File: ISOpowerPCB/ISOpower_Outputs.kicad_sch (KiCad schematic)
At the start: 53 parts

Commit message: deleted old backups & added documentation
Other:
- note added: "THis is all wrong, needs 12v drivers]"
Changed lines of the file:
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@@
     (effects (font (size 0.8 0.8)) (justify left bottom))
+  )
+  (text "THis is all wrong, needs 12v drivers]\n" (at 201.93 154.94 0)
+    (effects (font (size 2.5 2.5)) (justify left bottom))
   )
   (text "USB Control Logic" (at 40.64 71.12 0)

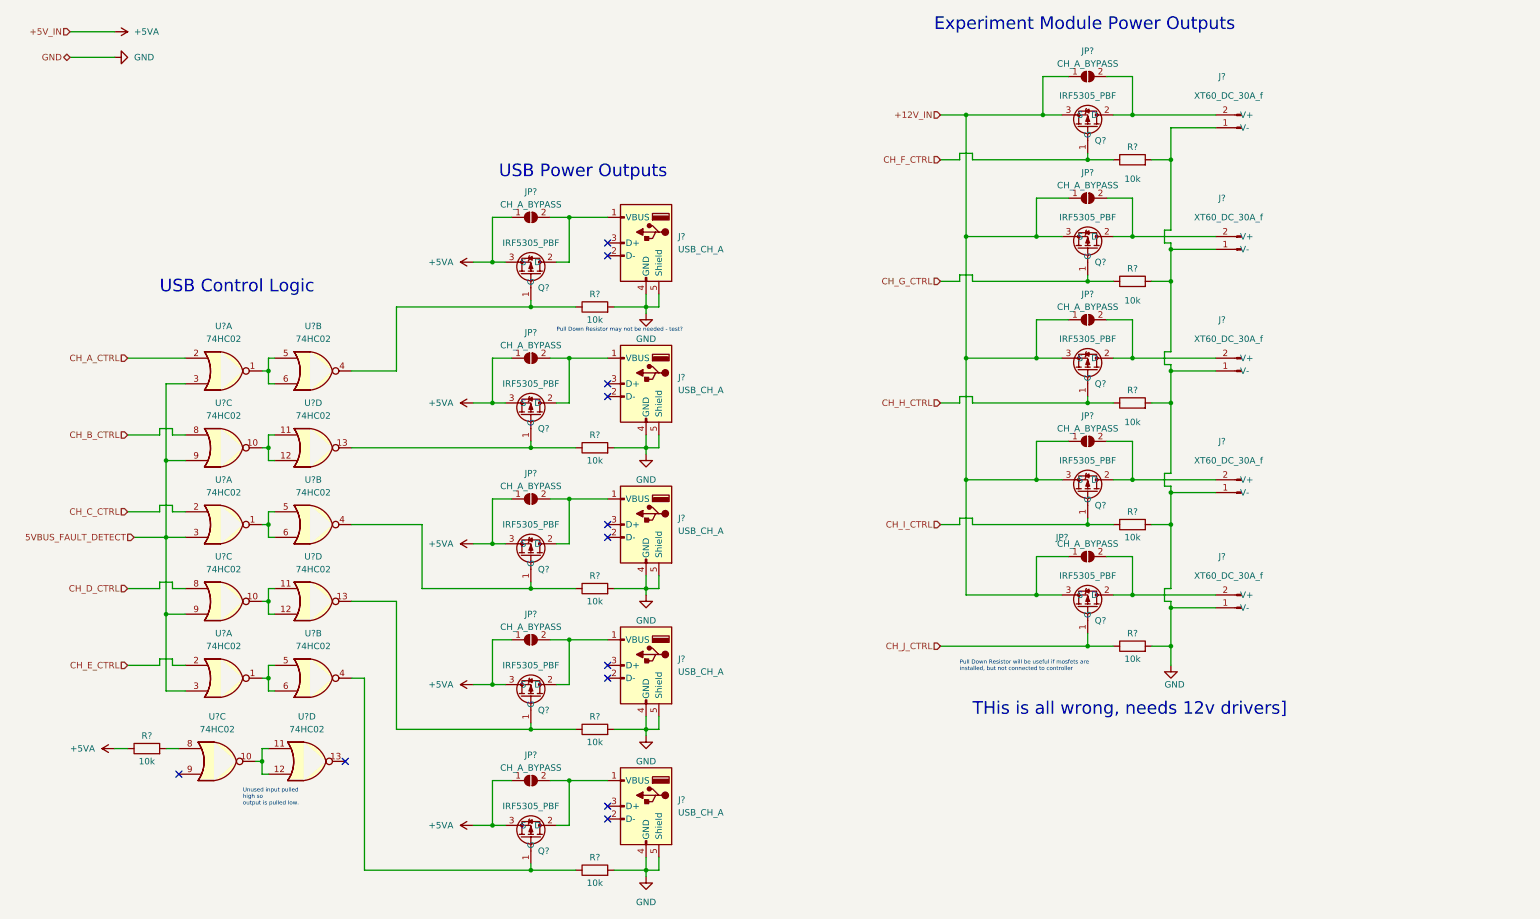
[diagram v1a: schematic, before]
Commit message: Finished initial circuit design
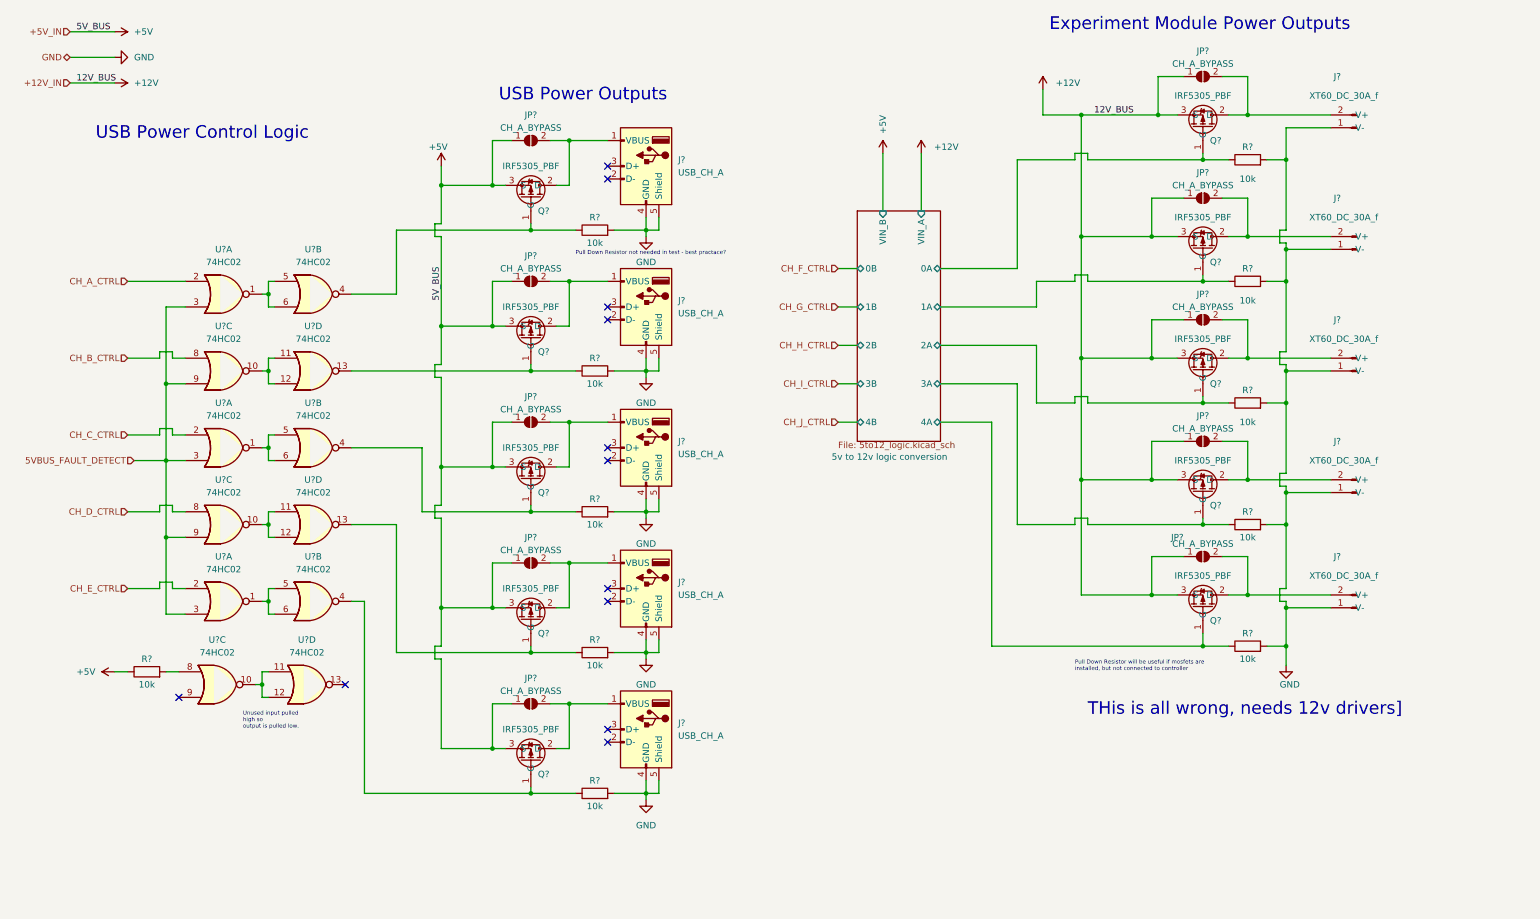
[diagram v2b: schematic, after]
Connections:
- net CH_F_CTRL: no longer Q?.1 (G), R?.1
- net CH_G_CTRL: no longer Q?.1 (G), R?.1
- net CH_H_CTRL: no longer Q?.1 (G), R?.1
- net CH_I_CTRL: no longer Q?.1 (G), R?.1
- net CH_J_CTRL: no longer Q?.1 (G), R?.1
- net +12V_IN renamed +12V
- net +5VA renamed +5V
- new net 5v to 12v logic conversion/0A: Q?.1 (G), R?.1
- new net 5v to 12v logic conversion/1A: Q?.1 (G), R?.1
- new net 5v to 12v logic conversion/2A: Q?.1 (G), R?.1
- new net 5v to 12v logic conversion/3A: Q?.1 (G), R?.1
- new net 5v to 12v logic conversion/4A: Q?.1 (G), R?.1
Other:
- added sheet 5v to 12v logic conversion (5to12_logic.kicad_sch)
- note added: "Pull Down Resistor not needed in test - best practace?"
- note added: "USB Power Control Logic"
- note removed: "Pull Down Resistor may not be needed - test?"
- note removed: "USB Control Logic"
- moved on the sheet: J?, JP?, Q?, R?, U?A, U?B, U?C, U?D

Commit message: Major schematic revisions
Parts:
- removed JP? (x5): CH_A_BYPASS, symbol Jumper:SolderJumper_2_Open
- removed Q? (x5): IRF5305_PBF, Package_TO_SOT_THT:TO-220-3_Vertical, symbol 000_MOSFET_Immo:IRF5305_PBF
- removed R? (x6): 10k, Resistor_SMD:R_0805_2012Metric_Pad1.20x1.40mm_HandSolder, symbol 000_Resistors_Immo:Resistor_0805
- removed U? (x12): 74HC02, symbol 74xx:74HC02
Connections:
- net +5V: now also J?.1 (VBUS), J?.1 (VBUS), J?.1 (VBUS), J?.1 (VBUS), J?.1 (VBUS)
- no-connect marks 12 -> 10
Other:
- note removed: "Pull Down Resistor not needed in test - best practace?"
- note removed: "USB Power Control Logic"
- note removed: "Unused input pulled high so output is pulled low."
- moved on the sheet: J?

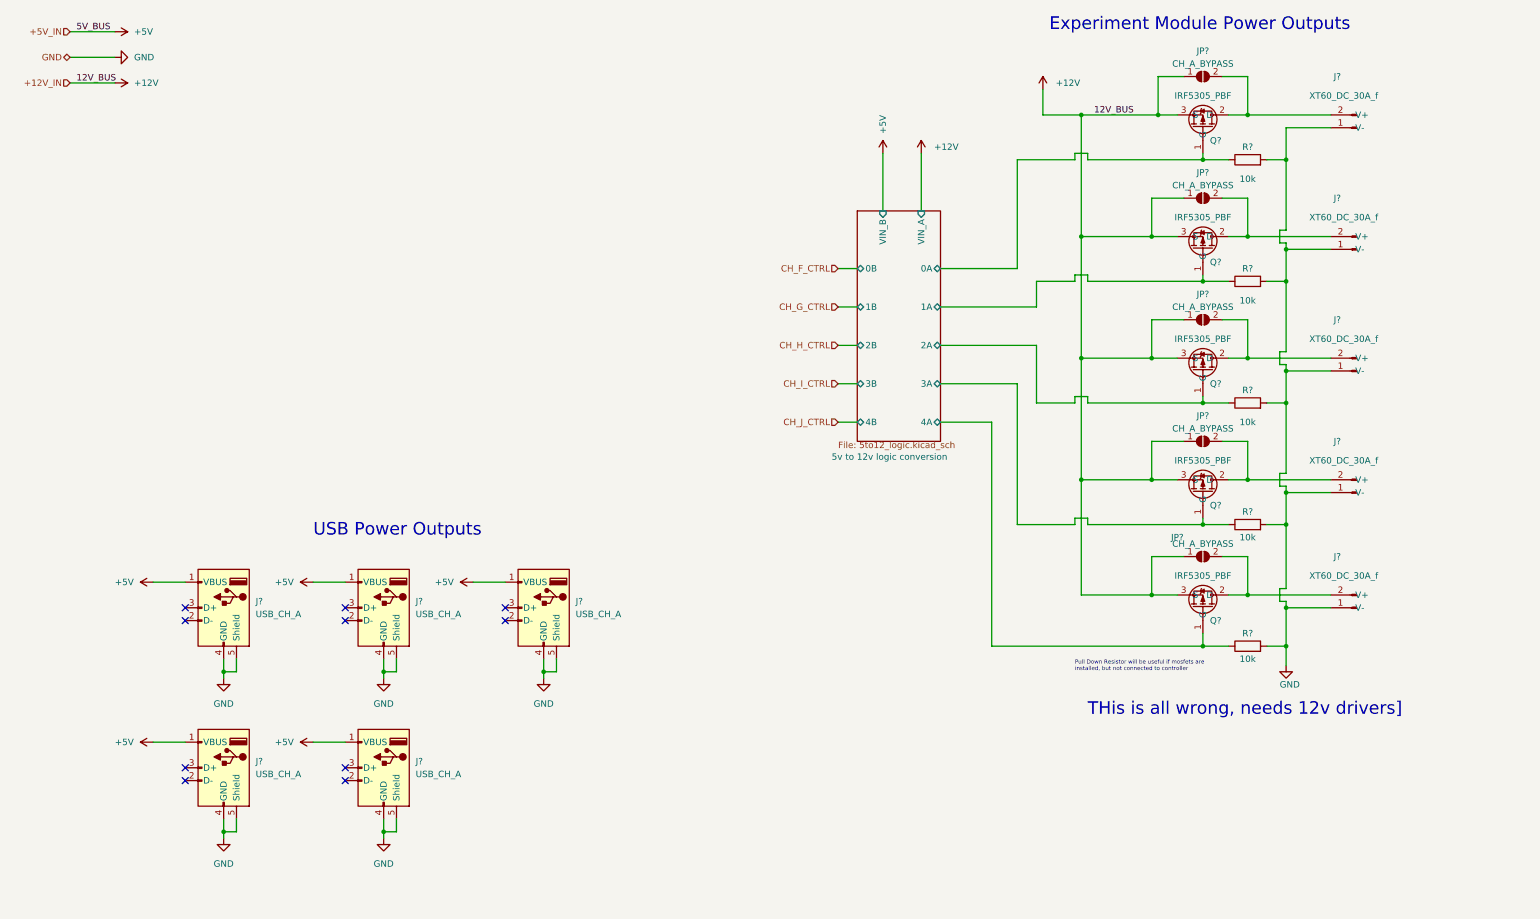
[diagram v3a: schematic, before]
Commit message: Updated as per discussions 26/01/22
# Change Notes

04/02/2022
As per discussion 26/01/22
1. Changed per channel 5v MOSFET switches to MOSFET control of DC/DC module on/off pin - due to failure of MOSFET switching during testing.
2. Added 5v buck converter for independent MCU_5V power bus.
	- Ensured all 5v MCU hardware is powered from common MCU_5V bus.
3. Removed circuit from NC pins on DC/DC modules.
4. Changed ESP32 USB interface to CH340
5. Changed MCU serial logic level converters from MOSFET to IC - TXS0102DCT
	- TODO: OE pin now requires low signal untill DC/DC supply is stable - Does it? Can it just be tied to 5v bus with a large capacitor? Does it need MCU to hold pin low untill 5V_BUS is stable?
6. Removed redundent 3V3_IN to power distribution page.
	- Rechecked all sheets for redundent pins, it won't impact drawing traces, but it will impact readability.
7. Added Mechanical layer as hirarchical sheet.
8. Moved voltage monitoring circuits to hirarchical sheet
9. Added voltage monitoring with TL431DBZ to 12V_BUS
10. Automatic shutoff circuit removed, as this would prevent the DC/DC module from powering on. Instead moved to AtMega328p digital inputs
and microcontroller will control shutdown of DC/DC supply if out of spec voltage detected.
		- This is a severe limitation compared to the specification, and this also does not prevent damage to devices on 5V_BUS if voltage is pulled high, for example to 12v due to user error.
		- TODO: Add independent overvoltage protection to 5V_BUS? 		[Zener Diode Overvoltage Protection - Sparkfun](https://www.rs-online.com/designspark/how-does-zener-diode-do-overvoltage-protection-in-circuit#:~:text=In%20order%20to%20protect%20the,flow%20in%20the%20reverse%20direction).
11. Changed logic level conversion for 12v outputs to 12v drive circuit. [12v drive circuit](https://forum.arduino.cc/t/easiest-way-of-driving-amplifying-from-5v-to-12v/123290)
12. Added proto pin connections for ESP MCU.
13. Changed 20v Zener in reverse vol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
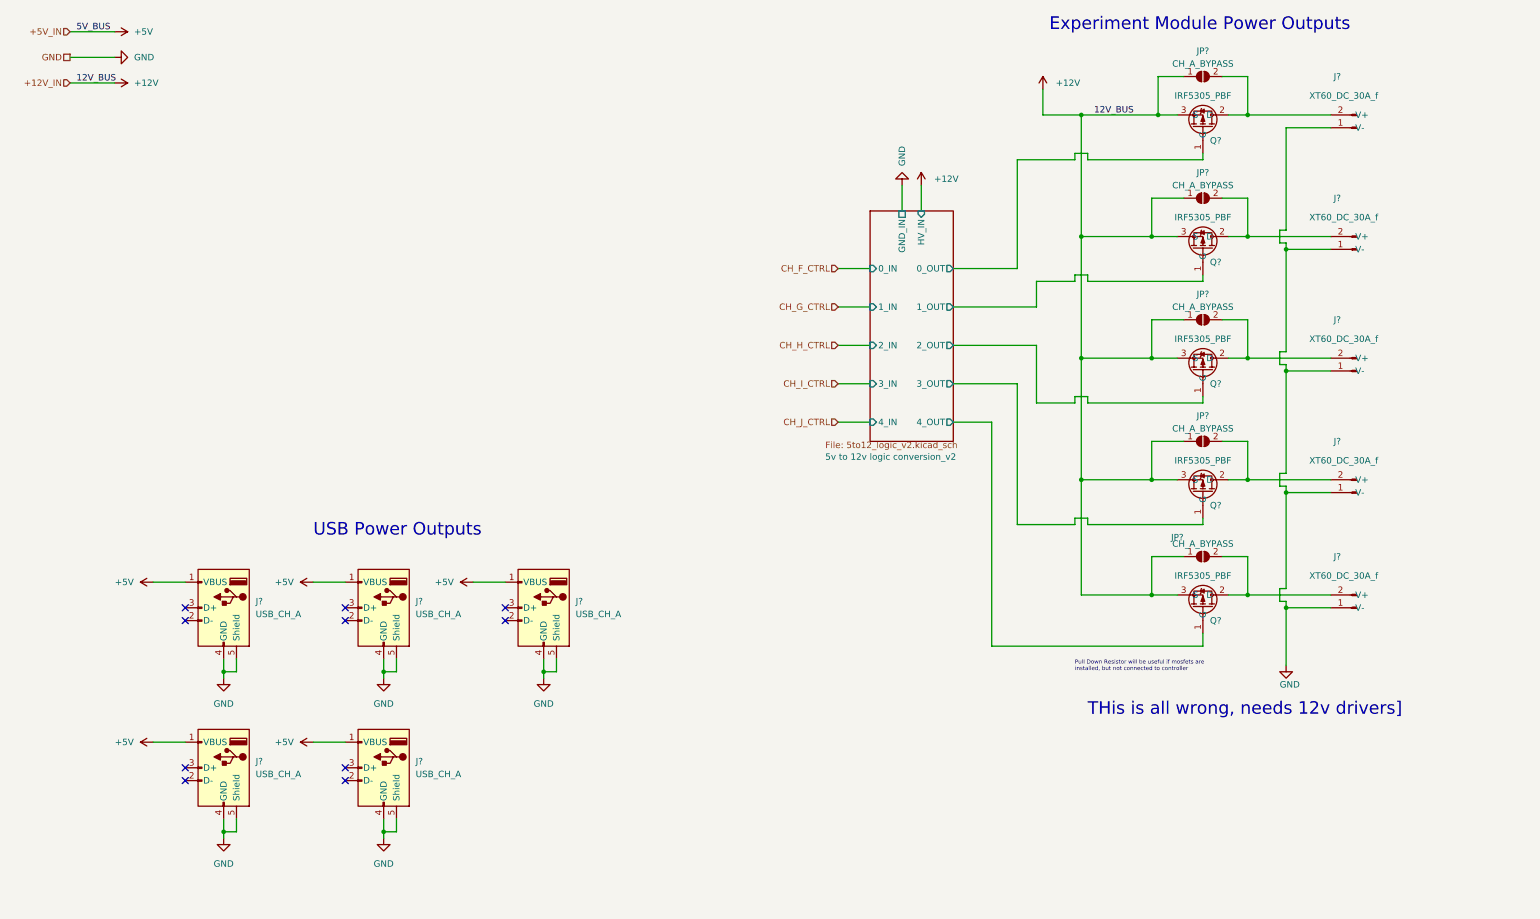
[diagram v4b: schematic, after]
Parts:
- removed R? (x5): 10k, Resistor_SMD:R_0805_2012Metric_Pad1.20x1.40mm_HandSolder, symbol 000_Resistors_Immo:Resistor_0805
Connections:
- net 5v to 12v logic conversion/0A renamed 5v to 12v logic conversion_v2/0_OUT
- net 5v to 12v logic conversion/1A renamed 5v to 12v logic conversion_v2/1_OUT
- net 5v to 12v logic conversion/2A renamed 5v to 12v logic conversion_v2/2_OUT
- net 5v to 12v logic conversion/3A renamed 5v to 12v logic conversion_v2/3_OUT
- net 5v to 12v logic conversion/4A renamed 5v to 12v logic conversion_v2/4_OUT
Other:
- removed sheet 5v to 12v logic conversion
- added sheet 5v to 12v logic conversion_v2 (5to12_logic_v2.kicad_sch)
